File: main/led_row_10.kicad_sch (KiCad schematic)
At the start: 30 parts

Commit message: Initial schematic complete
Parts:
- renumbered C82 to C301, C83 to C302, C84 to C303, C85 to C304, C86 to C305, C87 to C306, C88 to C307, C89 to C308, C90 to C309, C91 to C310, C92 to C311, C93 to C312, C94 to C313, C95 to C314, C96 to C?, D154 to D301, D155 to D302, D156 to D303, D157 to D304, D158 to D305, D159 to D306, D160 to D307, D161 to D308, D162 to D309, D163 to D310, D164 to D311, D165 to D312, D166 to D313, D167 to D314, D168 to D?

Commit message: Start placing components
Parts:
- C82: renamed from C301; footprint (none) -> Capacitor_SMD:C_0603_1608Metric
- C83: renamed from C302; footprint (none) -> Capacitor_SMD:C_0603_1608Metric
- C84: renamed from C303; footprint (none) -> Capacitor_SMD:C_0603_1608Metric
- C85: renamed from C304; footprint (none) -> Capacitor_SMD:C_0603_1608Metric
- C86: renamed from C305; footprint (none) -> Capacitor_SMD:C_0603_1608Metric
- C87: renamed from C306; footprint (none) -> Capacitor_SMD:C_0603_1608Metric
- C88: renamed from C307; footprint (none) -> Capacitor_SMD:C_0603_1608Metric
- C89: renamed from C308; footprint (none) -> Capacitor_SMD:C_0603_1608Metric
- C90: renamed from C309; footprint (none) -> Capacitor_SMD:C_0603_1608Metric
- C91: renamed from C310; footprint (none) -> Capacitor_SMD:C_0603_1608Metric
- C92: renamed from C311; footprint (none) -> Capacitor_SMD:C_0603_1608Metric
- C93: renamed from C312; footprint (none) -> Capacitor_SMD:C_0603_1608Metric
- C94: renamed from C313; footprint (none) -> Capacitor_SMD:C_0603_1608Metric
- C95: renamed from C314; footprint (none) -> Capacitor_SMD:C_0603_1608Metric
- C96: renamed from C?; footprint (none) -> Capacitor_SMD:C_0603_1608Metric
- D154: renamed from D301; footprint bigbutton:LED_SK6812_MINI_E_REVERSE -> chonc60:LED_SK6812_MINI_E_REVERSE
- D155: renamed from D302; footprint bigbutton:LED_SK6812_MINI_E_REVERSE -> chonc60:LED_SK6812_MINI_E_REVERSE
- D156: renamed from D303; footprint bigbutton:LED_SK6812_MINI_E_REVERSE -> chonc60:LED_SK6812_MINI_E_REVERSE
- D157: renamed from D304; footprint bigbutton:LED_SK6812_MINI_E_REVERSE -> chonc60:LED_SK6812_MINI_E_REVERSE
- D158: renamed from D305; footprint bigbutton:LED_SK6812_MINI_E_REVERSE -> chonc60:LED_SK6812_MINI_E_REVERSE
- D159: renamed from D306; footprint bigbutton:LED_SK6812_MINI_E_REVERSE -> chonc60:LED_SK6812_MINI_E_REVERSE
- D160: renamed from D307; footprint bigbutton:LED_SK6812_MINI_E_REVERSE -> chonc60:LED_SK6812_MINI_E_REVERSE
- D161: renamed from D308; footprint bigbutton:LED_SK6812_MINI_E_REVERSE -> chonc60:LED_SK6812_MINI_E_REVERSE
- D162: renamed from D309; footprint bigbutton:LED_SK6812_MINI_E_REVERSE -> chonc60:LED_SK6812_MINI_E_REVERSE
- D163: renamed from D310; footprint bigbutton:LED_SK6812_MINI_E_REVERSE -> chonc60:LED_SK6812_MINI_E_REVERSE
- D164: renamed from D311; footprint bigbutton:LED_SK6812_MINI_E_REVERSE -> chonc60:LED_SK6812_MINI_E_REVERSE
- D165: renamed from D312; footprint bigbutton:LED_SK6812_MINI_E_REVERSE -> chonc60:LED_SK6812_MINI_E_REVERSE
- D166: renamed from D313; footprint bigbutton:LED_SK6812_MINI_E_REVERSE -> chonc60:LED_SK6812_MINI_E_REVERSE
- D167: renamed from D314; footprint bigbutton:LED_SK6812_MINI_E_REVERSE -> chonc60:LED_SK6812_MINI_E_REVERSE
- D168: renamed from D?; footprint bigbutton:LED_SK6812_MINI_E_REVERSE -> chonc60:LED_SK6812_MINI_E_REVERSE

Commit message: Start placing diodes
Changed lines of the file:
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@@
   )
   (symbol (lib_id "power:GND") (at 262.89 36.83 0) (unit 1)
-    (in_bom yes) (on_board yes)
-    (property "Reference" "#PWR0273" (id 0) (at 262.89 43.18 0)
-      (effects (font (size 1.27 1.27)) hide)
-    )
-    (property "Value" "GND" (id 1) (at 263.0043 41.1544 0))
+    (in_bom yes) (on_board yes) (fields_autoplaced)
+    (property "Reference" "#PWR053" (id 0) (at 262.89 43.18 0)
+      (effects (font (size 1.27 1.27)) hide)
+    )
+    (property "Value" "GND" (id 1) (at 262.89 41.1544 0))
     (property "Footprint" "" (id 2) (at 262.89 36.83 0)
       (effects (font (size 1.27 1.27)) hide)
@@
     (pin "4")
   )
-  (symbol (lib_id "chonc60:SK6812MINI-E") (at 34.29 26.67 0) (unit 1)
+  (symbol (lib_name "chonc60:SK6812MINI-E_14") (lib_id "chonc60:SK6812MINI-E") (at 34.29 26.67 0) (unit 1)
     (in_bom yes) (on_board yes)
     (property "Reference" "D154" (id 0) (at 37.8461 17.9006 0)
@@
     (pin "4")
   )
-  (symbol (lib_id "chonc60:SK6812MINI-E") (at 58.42 63.5 0) (unit 1)
+  (symbol (lib_name "chonc60:SK6812MINI-E_12") (lib_id "chonc60:SK6812MINI-E") (at 58.42 63.5 0) (unit 1)
     (in_bom yes) (on_board yes)
     (property "Reference" "D165" (id 0) (at 61.9761 54.7306 0)
@@
     (pin "4")
   )
-  (symbol (lib_id "chonc60:SK6812MINI-E") (at 59.69 26.67 0) (unit 1)
+  (symbol (lib_name "chonc60:SK6812MINI-E_11") (lib_id "chonc60:SK6812MINI-E") (at 59.69 26.67 0) (unit 1)
     (in_bom yes) (on_board yes)
     (property "Reference" "D155" (id 0) (at 63.2461 17.9006 0)
@@
     (pin "4")
   )
-  (symbol (lib_id "chonc60:SK6812MINI-E") (at 83.82 63.5 0) (unit 1)
+  (symbol (lib_name "chonc60:SK6812MINI-E_13") (lib_id "chonc60:SK6812MINI-E") (at 83.82 63.5 0) (unit 1)
     (in_bom yes) (on_board yes)
     (property "Reference" "D166" (id 0) (at 87.3761 54.7306 0)
@@
     (pin "4")
   )
-  (symbol (lib_id "chonc60:SK6812MINI-E") (at 85.09 26.67 0) (unit 1)
+  (symbol (lib_name "chonc60:SK6812MINI-E_10") (lib_id "chonc60:SK6812MINI-E") (at 85.09 26.67 0) (unit 1)
     (in_bom yes) (on_board yes)
     (property "Reference" "D156" (id 0) (at 88.6461 17.9006 0)
@@
     (pin "4")
   )
-  (symbol (lib_id "chonc60:SK6812MINI-E") (at 109.22 63.5 0) (unit 1)
+  (symbol (lib_name "chonc60:SK6812MINI-E_2") (lib_id "chonc60:SK6812MINI-E") (at 109.22 63.5 0) (unit 1)
     (in_bom yes) (on_board yes)
     (property "Reference" "D167" (id 0) (at 112.7761 54.7306 0)
@@
     (pin "4")
   )
-  (symbol (lib_id "chonc60:SK6812MINI-E") (at 110.49 26.67 0) (unit 1)
+  (symbol (lib_name "chonc60:SK6812MINI-E_7") (lib_id "chonc60:SK6812MINI-E") (at 110.49 26.67 0) (unit 1)
     (in_bom yes) (on_board yes)
     (property "Reference" "D157" (id 0) (at 114.0461 17.9006 0)
@@
     (pin "4")
   )
-  (symbol (lib_id "chonc60:SK6812MINI-E") (at 135.89 26.67 0) (unit 1)
+  (symbol (lib_name "chonc60:SK6812MINI-E_8") (lib_id "chonc60:SK6812MINI-E") (at 135.89 26.67 0) (unit 1)
     (in_bom yes) (on_board yes)
     (property "Reference" "D158" (id 0) (at 139.4461 17.9006 0)
@@
     (pin "4")
   )
-  (symbol (lib_id "chonc60:SK6812MINI-E") (at 135.89 63.5 0) (unit 1)
+  (symbol (lib_name "chonc60:SK6812MINI-E_1") (lib_id "chonc60:SK6812MINI-E") (at 135.89 63.5 0) (unit 1)
     (in_bom yes) (on_board yes)
     (property "Reference" "D168" (id 0) (at 139.4461 54.7306 0)
@@
     (pin "4")
   )
-  (symbol (lib_id "chonc60:SK6812MINI-E") (at 161.29 26.67 0) (unit 1)
+  (symbol (lib_name "chonc60:SK6812MINI-E_6") (lib_id "chonc60:SK6812MINI-E") (at 161.29 26.67 0) (unit 1)
     (in_bom yes) (on_board yes)
     (property "Reference" "D159" (id 0) (at 164.8461 17.9006 0)
@@
     (pin "4")
   )
-  (symbol (lib_id "chonc60:SK6812MINI-E") (at 186.69 26.67 0) (unit 1)
+  (symbol (lib_name "chonc60:SK6812MINI-E_9") (lib_id "chonc60:SK6812MINI-E") (at 186.69 26.67 0) (unit 1)
     (in_bom yes) (on_board yes)
     (property "Reference" "D160" (id 0) (at 190.2461 17.9006 0)
@@
     (pin "4")
   )
-  (symbol (lib_id "chonc60:SK6812MINI-E") (at 212.09 26.67 0) (unit 1)
+  (symbol (lib_name "chonc60:SK6812MINI-E_3") (lib_id "chonc60:SK6812MINI-E") (at 212.09 26.67 0) (unit 1)
     (in_bom yes) (on_board yes)
     (property "Reference" "D161" (id 0) (at 215.6461 17.9006 0)
@@
     (pin "4")
   )
-  (symbol (lib_id "chonc60:SK6812MINI-E") (at 237.49 26.67 0) (unit 1)
+  (symbol (lib_name "chonc60:SK6812MINI-E_5") (lib_id "chonc60:SK6812MINI-E") (at 237.49 26.67 0) (unit 1)
     (in_bom yes) (on_board yes)
     (property "Reference" "D162" (id 0) (at 241.0461 17.9006 0)
@@
     (pin "4")
   )
-  (symbol (lib_id "chonc60:SK6812MINI-E") (at 262.89 26.67 0) (unit 1)
+  (symbol (lib_name "chonc60:SK6812MINI-E_4") (lib_id "chonc60:SK6812MINI-E") (at 262.89 26.67 0) (unit 1)
     (in_bom yes) (on_board yes)
     (property "Reference" "D163" (id 0) (at 266.4461 17.9006 0)

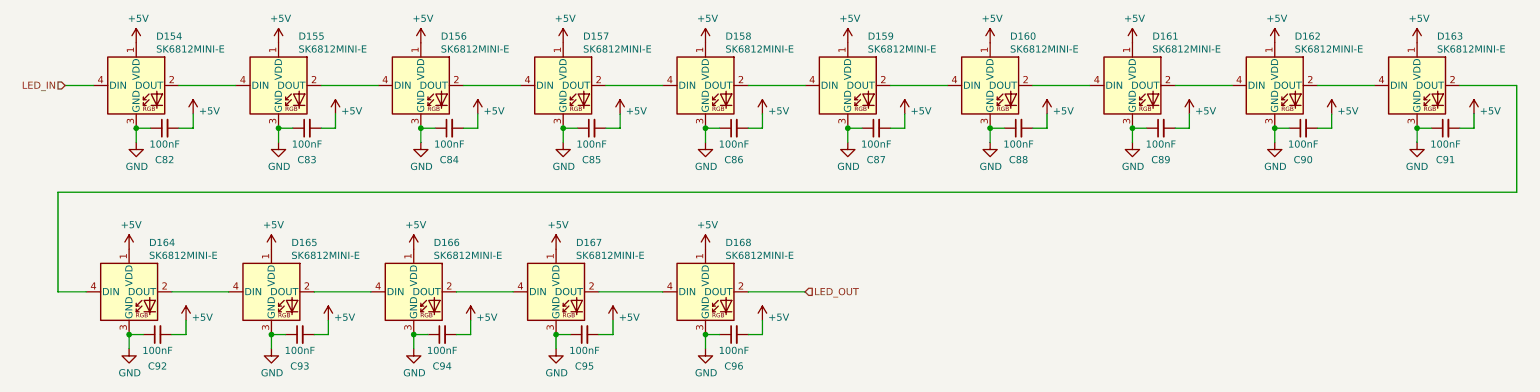
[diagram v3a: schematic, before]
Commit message: Place diodes
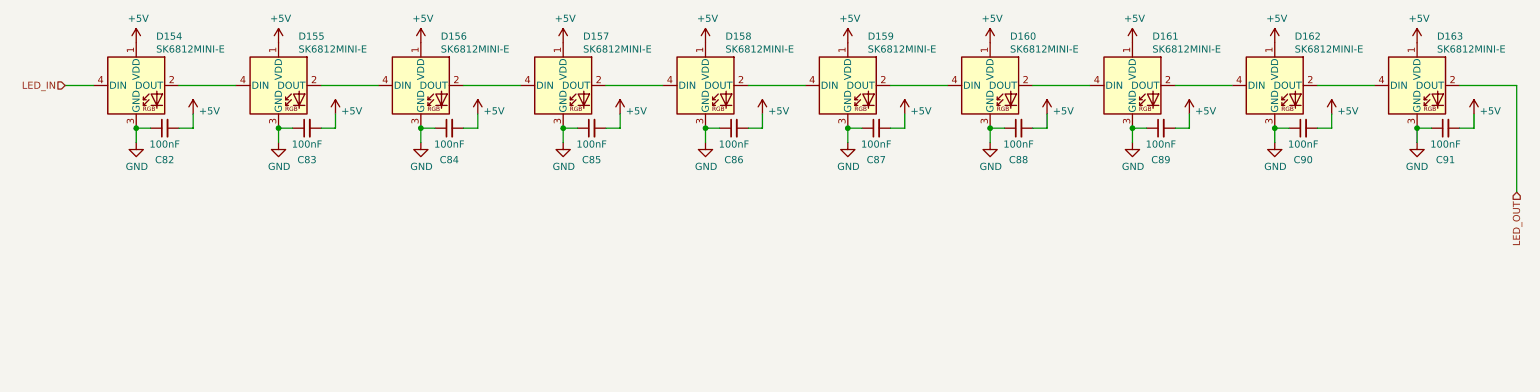
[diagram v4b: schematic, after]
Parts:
- removed C92, C93, C94, C95, C96: 100nF, Capacitor_SMD:C_0603_1608Metric, symbol Device:C_Small
- removed D164, D165, D166, D167, D168: SK6812MINI-E, chonc60:LED_SK6812_MINI_E_REVERSE, symbol chonc60:SK6812MINI-E
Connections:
- net LED_OUT: now also D163.2 (DOUT)

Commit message: Place LEDs, start routing
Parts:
- renumbered C82 to C75, C83 to C76, C84 to C77, C85 to C78, C86 to C79, C87 to C80, C88 to C81, C89 to C82, C90 to C83, C91 to C84, D154 to D147, D155 to D148, D156 to D149, D157 to D150, D158 to D151, D159 to D152, D160 to D153, D161 to D154, D162 to D155, D163 to D156
